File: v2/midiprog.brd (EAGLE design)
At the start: 99.1 x 78.7 mm, 56 parts, among them IC1 PIC18F4550_40, IC2 TPIC6B596N, IC4 TPIC6B596N, Q2 2N2222A, Q3 2N2222A, Q4 2N2222A, Q5 8MHz

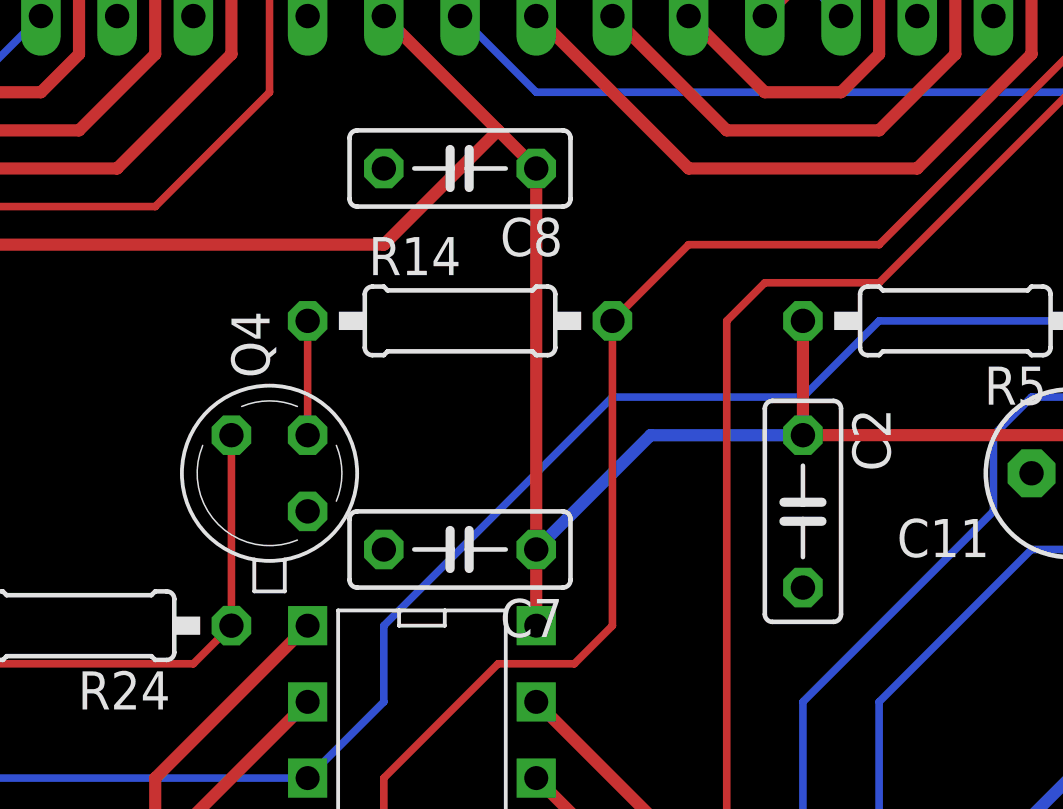
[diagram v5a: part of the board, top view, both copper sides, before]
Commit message: Uncramped parts.
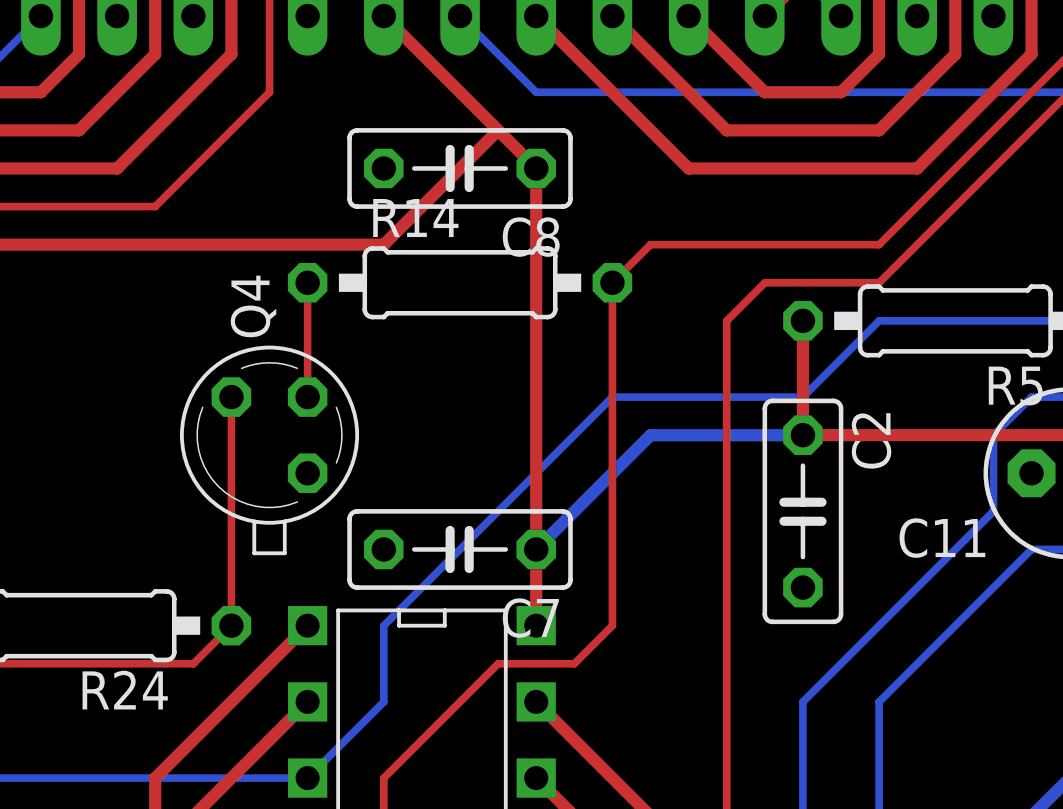
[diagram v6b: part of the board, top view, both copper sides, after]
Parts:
- moved Q4 1.27 mm to (30.5, 35.6)
- moved R14 1.27 mm to (36.8, 40.6)
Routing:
- net N$54: track 38.2 -> 39.5 mm
- net BTN_S3: track 61.5 -> 62.3 mm
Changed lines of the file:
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@@
 <element name="U$2" library="joe" package="CD74HC4051E" value="CD74HC4051E" x="16.51" y="19.05" rot="R270"/>
 <element name="ICD" library="con-amp-quick" package="05PA" value="" x="69.85" y="68.58"/>
-<element name="Q4" library="transistor-npn" package="TO18" value="2N2222A" x="30.48" y="34.29" rot="R90"/>
-<element name="R14" library="rcl" package="0207/10" value="10K" x="36.83" y="39.37"/>
+<element name="Q4" library="transistor-npn" package="TO18" value="2N2222A" x="30.48" y="35.56" rot="R90"/>
+<element name="R14" library="rcl" package="0207/10" value="10K" x="36.83" y="40.64"/>
 <element name="R24" library="rcl" package="0207/10" value="10k" x="24.13" y="29.21" rot="R180"/>
 <element name="BTN_FX_CN" library="con-lstb" package="MA08-2" value="" x="12.7" y="7.62" rot="R180">
@@
 <wire x1="41.91" y1="29.21" x2="40.64" y2="27.94" width="0.254" layer="1"/>
 <wire x1="40.64" y1="27.94" x2="38.1" y2="27.94" width="0.254" layer="1"/>
-<wire x1="41.91" y1="39.37" x2="41.91" y2="29.21" width="0.254" layer="1"/>
+<wire x1="41.91" y1="40.64" x2="41.91" y2="29.21" width="0.254" layer="1"/>
 <wire x1="57.15" y1="50.8" x2="63.5" y2="57.15" width="0.254" layer="1"/>
 <wire x1="57.15" y1="48.26" x2="57.15" y2="50.8" width="0.254" layer="1"/>
 <wire x1="50.8" y1="41.91" x2="57.15" y2="48.26" width="0.254" layer="1"/>
-<wire x1="44.45" y1="41.91" x2="50.8" y2="41.91" width="0.254" layer="1"/>
-<wire x1="41.91" y1="39.37" x2="44.45" y2="41.91" width="0.254" layer="1"/>
+<wire x1="43.18" y1="41.91" x2="50.8" y2="41.91" width="0.254" layer="1"/>
+<wire x1="41.91" y1="40.64" x2="43.18" y2="41.91" width="0.254" layer="1"/>
 </signal>
 <signal name="GND">
@@
 <contactref element="Q4" pad="2"/>
 <contactref element="R14" pad="1"/>
-<wire x1="31.75" y1="39.37" x2="31.75" y2="35.56" width="0.254" layer="1"/>
+<wire x1="31.75" y1="40.64" x2="31.75" y2="36.83" width="0.254" layer="1"/>
 </signal>
 <signal name="N$54">
@@
 <contactref element="Q4" pad="3"/>
 <contactref element="R24" pad="1"/>
-<wire x1="29.21" y1="29.21" x2="29.21" y2="35.56" width="0.254" layer="1"/>
+<wire x1="29.21" y1="29.21" x2="29.21" y2="36.83" width="0.254" layer="1"/>
 <wire x1="8.89" y1="16.51" x2="7.62" y2="17.78" width="0.254" layer="1"/>
 <wire x1="7.62" y1="17.78" x2="7.62" y2="20.32" width="0.254" layer="1"/>

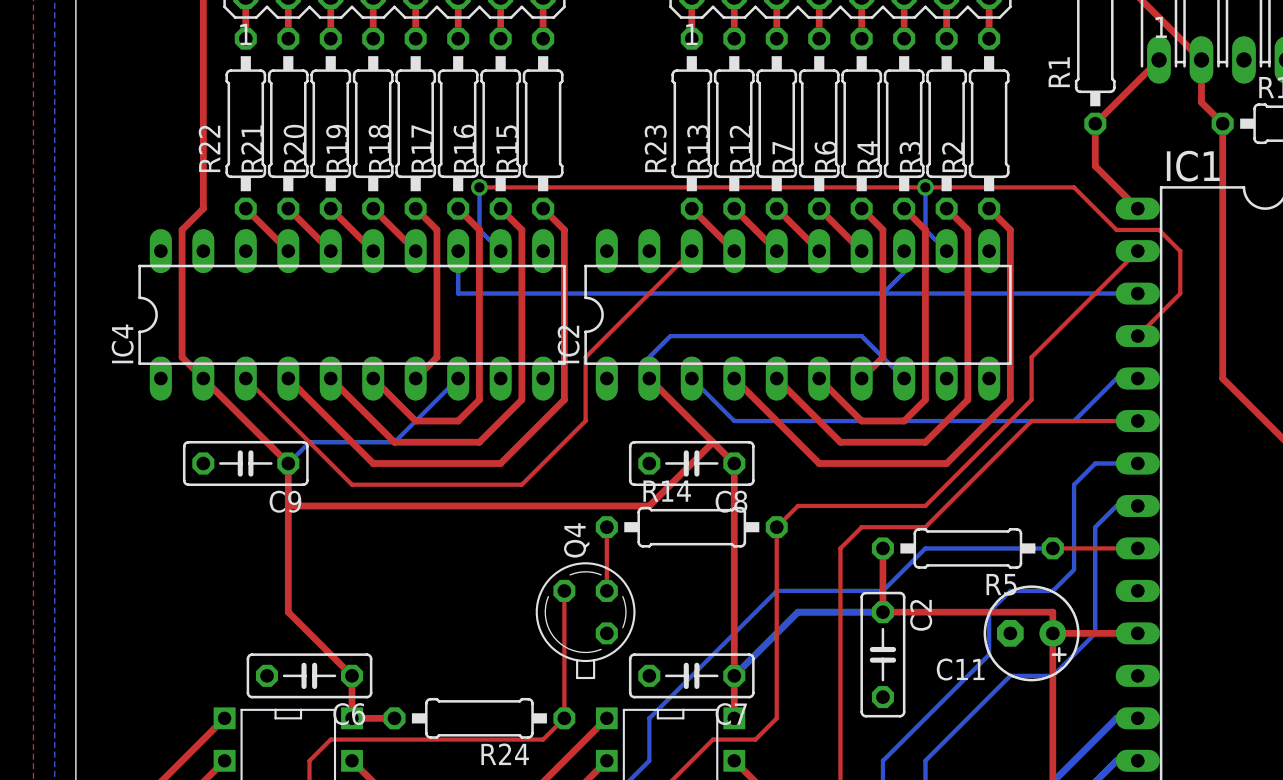
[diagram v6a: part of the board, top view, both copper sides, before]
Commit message: WIP on routing PIC to TPICs.
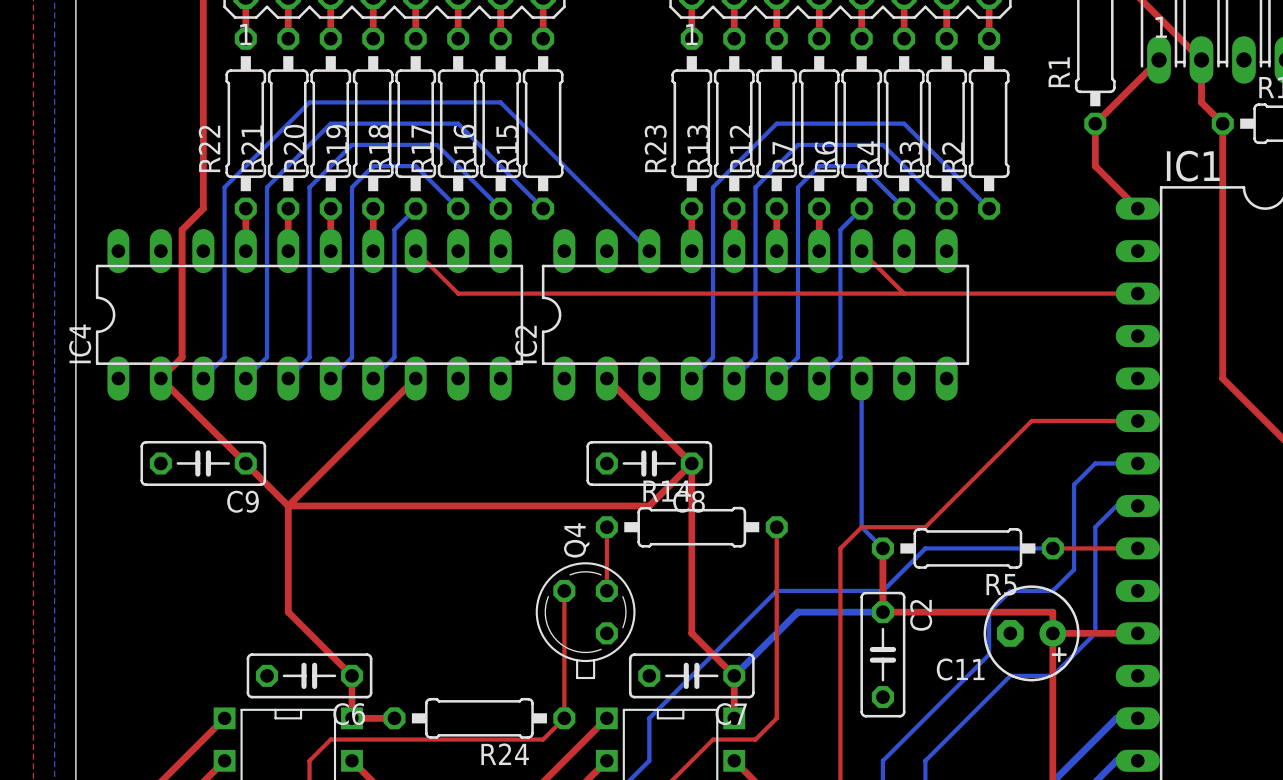
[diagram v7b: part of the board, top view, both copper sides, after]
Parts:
- moved IC4 2.54 mm to (14.0, 53.3)
- moved C9 2.54 mm to (7.62, 44.5)
- moved C8 2.54 mm to (34.3, 44.5)
- moved IC2 2.54 mm to (40.6, 53.3)
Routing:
- net SHIFTREG_RCK: track 58.3 -> 0.00 mm, vias 2 -> 0
- net BTN_S3: track 62.3 -> 32.4 mm
- net SHIFTREG_D: track 28.8 -> 0.00 mm
- net VDD: track 296.8 -> 288.2 mm
- net N$31: track 37.3 -> 43.1 mm
- net SHIFTREG_SCL: track 46.2 -> 47.8 mm
- net N$43: track 3.59 -> 2.54 mm
- net N$26: track 3.59 -> 2.54 mm
- net N$25: track 3.59 -> 2.54 mm
- net N$45: track 3.59 -> 2.54 mm
- net N$44: track 3.59 -> 2.54 mm
- net N$42: track 3.59 -> 2.54 mm
- net N$29: track 3.59 -> 2.54 mm
- net N$23: track 3.59 -> 2.54 mm

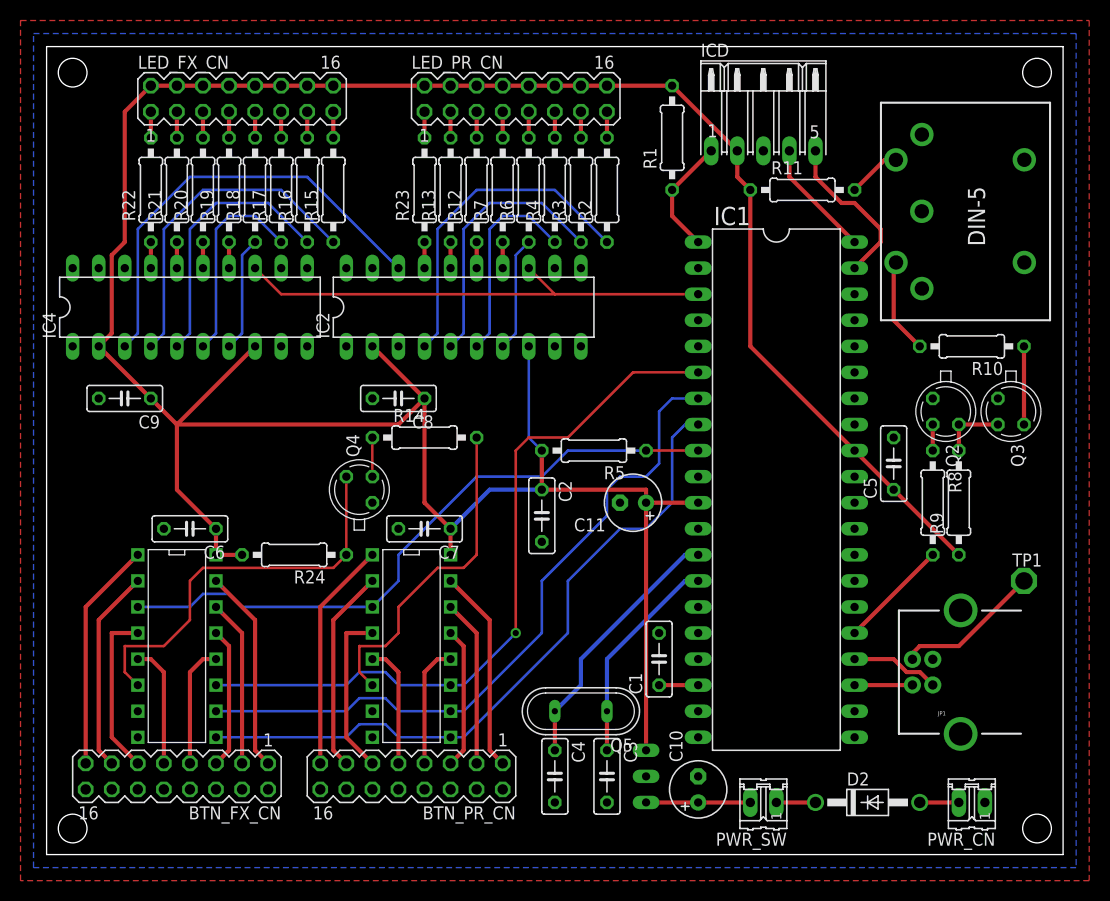
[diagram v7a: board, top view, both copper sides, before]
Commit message: Removed nearly all vias.
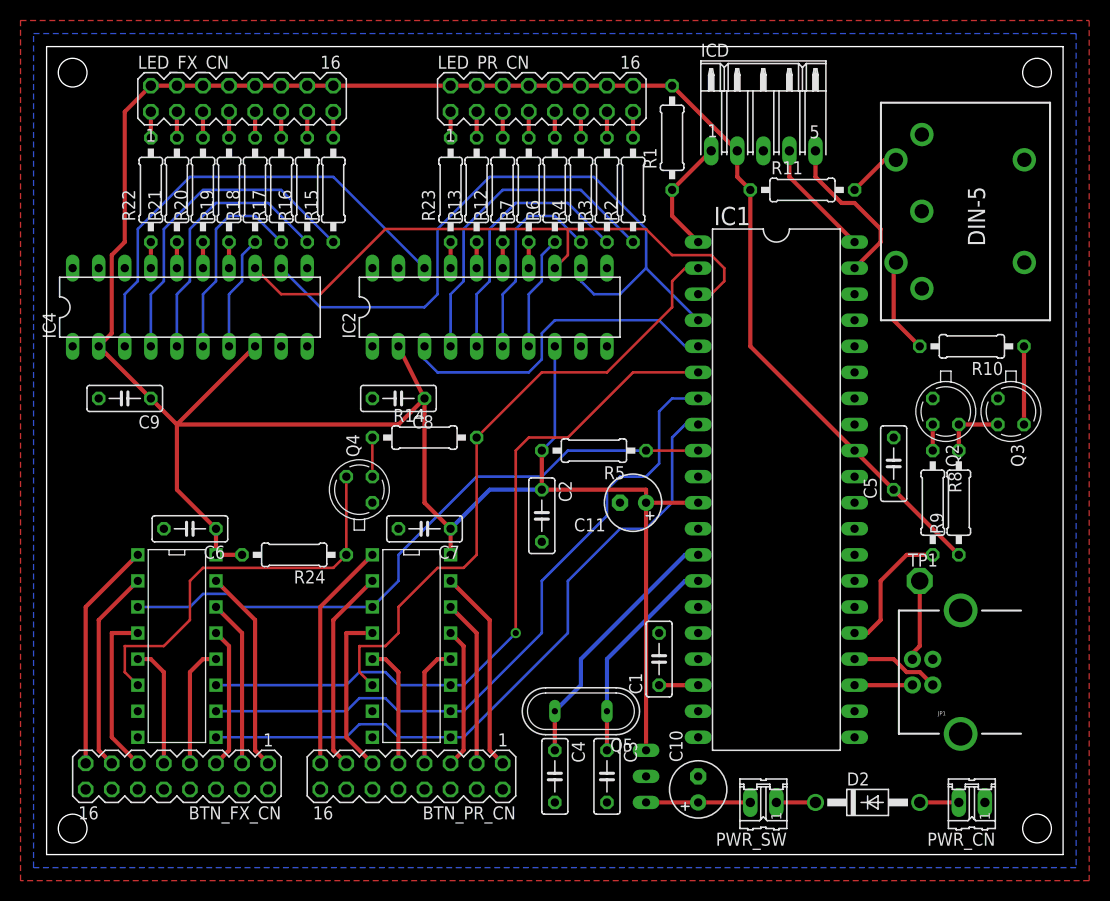
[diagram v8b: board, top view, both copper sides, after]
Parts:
- moved TP1 10.2 mm to (85.1, 26.7)
- moved R12 2.54 mm to (44.5, 64.8)
- moved IC2 2.54 mm to (43.2, 53.3)
- moved LED_PR_CN 2.54 mm to (48.3, 73.7)
- moved R13 2.54 mm to (41.9, 64.8)
- moved R2 2.54 mm to (57.1, 64.8)
- moved R23 2.54 mm to (39.4, 64.8)
- moved R3 2.54 mm to (54.6, 64.8)
- moved R4 2.54 mm to (52.1, 64.8)
- moved R6 2.54 mm to (49.5, 64.8)
- moved R7 2.54 mm to (47.0, 64.8)
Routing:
- net SHIFTREG_RCK: track 0.00 -> 68.4 mm
- net SHIFTREG_D: track 0.00 -> 33.1 mm
- net BTN_S3: track 32.4 -> 62.3 mm
- net SHIFTREG_SCL: track 47.8 -> 59.7 mm
- net USB_VCC: track 14.4 -> 7.93 mm
- net N$31: track 43.1 -> 45.7 mm
- net MIDI_TX: track 10.8 -> 13.0 mm
- net VDD: track 288.2 -> 286.7 mm
